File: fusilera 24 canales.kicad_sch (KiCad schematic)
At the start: 28 parts, among them J1 +12V borne M6, J2 GND borne M5, U4 MCP23017-E/SO, U5 MCP23017-E/SO, U6 LM5164DDA, U7 AP2112K-3.3

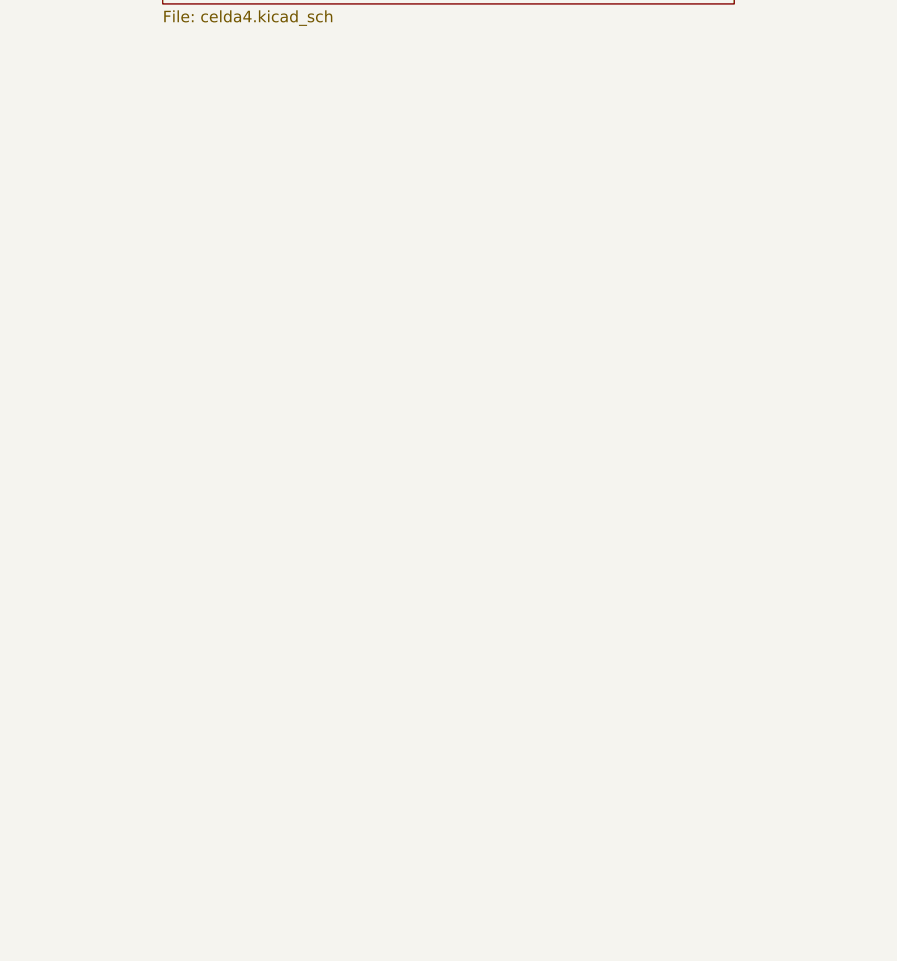
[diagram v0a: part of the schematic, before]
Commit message: Añade las celdas 4 y 5 de la cara inferior como copias volteadas en B.Cu
Agrega las hojas Celda4 y Celda5 al esquemático raíz (referencias +300 y +400,
pines sin cablear) y crea sus 87 footprints cada una en B.Cu como imagen en
espejo de la celda dorada, con 556 pistas y 101 vías, aparcadas bajo el
contorno. Con las siete celdas previstas (3 en la cara frontal, 4 en la
inferior) quedan 28 canales: el cuarto canal de la Celda5 y las celdas 6 y 7
serán las salidas directas. Se documenta el plan en CONTEXTO_PROYECTO.md.
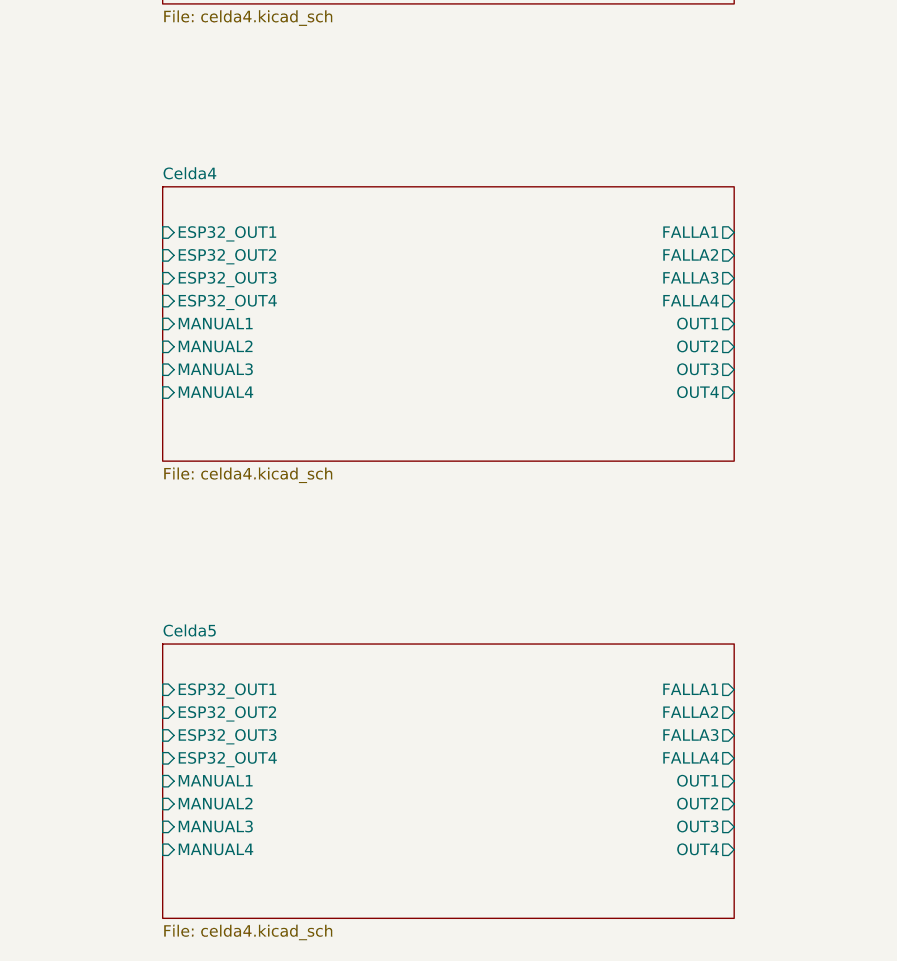
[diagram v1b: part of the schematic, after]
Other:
- added sheet Celda4 (celda4.kicad_sch)
- added sheet Celda5 (celda4.kicad_sch)

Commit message: Añade las celdas 6 y 7 (canales directos) y alarga la placa 47,7 mm
Hojas Celda6 y Celda7 en el esquemático con los canales idénticos a los demás;
los ESP32_OUT de las 9 salidas directas (canal 4 de la Celda5 y las celdas 6 y 7)
se amarran a +3,3 V en la raíz. En el PCB se alarga el contorno, los planos y las
tiras de +12 V; la Celda6 va en el frente como copia de la Celda3 y la Celda7 en B.Cu
colocada y ruteada con vías libres en todas las capas, con puentes en las islas del
plano +3,3 V. Quedan 3 conexiones sin rutear en la Celda7 y las uniones de +12 V
del reverso. Se documenta en CONTEXTO_PROYECTO.md.
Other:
- added sheet Celda6 (celda4.kicad_sch)
- added sheet Celda7 (celda4.kicad_sch)
